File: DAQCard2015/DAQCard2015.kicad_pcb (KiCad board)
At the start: 4 copper layers, 160 x 160 mm, 191 parts, among them CON1 BARREL_JACK, K1 1462042-8, P1 QTH-090-01-F-D-A, P2 QTH-090-01-F-D-A, P3 miniDIL20, P4 LEMO_EPY.00.250.NTN, P5 LEMO_EPY.00.250.NTN, P6 FAN, P7 CONN_02X20_Double, P9 SHV, Q1 MMBT2222A-TP, Q2 SBC817-40LT1G, SW1 DPDT, U1 RJ45x8, U10 AD9219, U11 THS4524IDBTR, U12 AD9219, U13 THS4524IDBTR, U14 AD9219, U15 THS4524IDBTR, U16 AD9219, U17 THS4524IDBTR, U18 AD9219, U19 AD8534, U2 AD5628, U20 LM1086, U21 LT1913, U22 AD5628, U23 AD8534, U24 MCP65R41, U3 THS4524IDBTR, U4 AD9219, U5 THS4524IDBTR, U6 AD9219, U7 THS4524IDBTR, U8 AD9219, U9 THS4524IDBTR

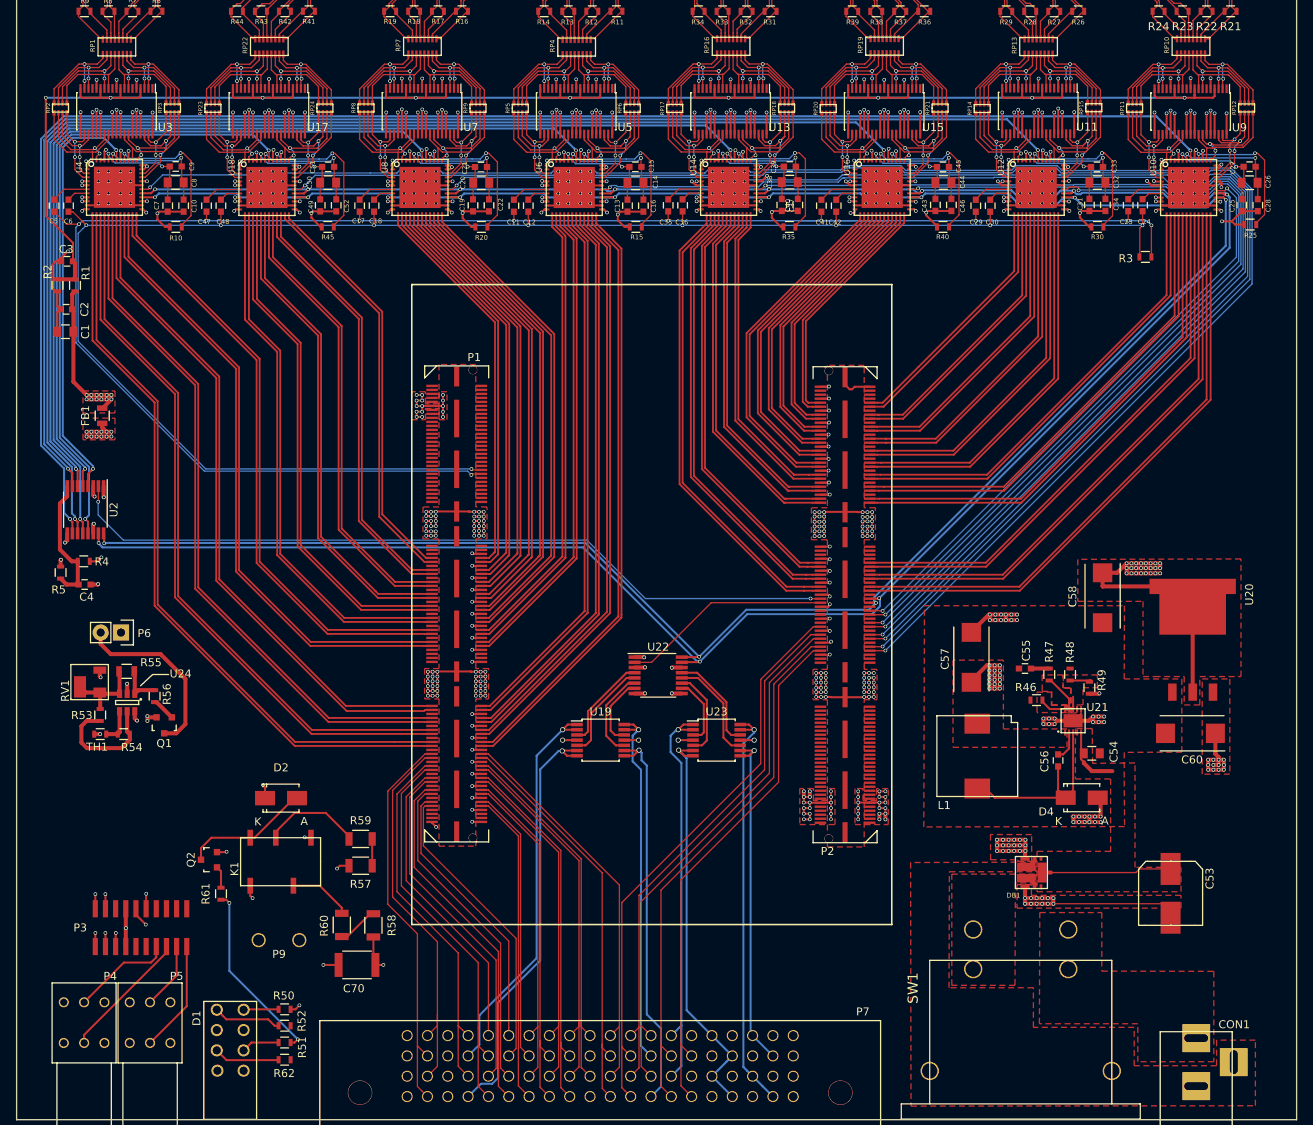
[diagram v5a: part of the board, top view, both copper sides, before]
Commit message: Update to DAQ Board including adding an JTAG header and hooking up external clock and trigger
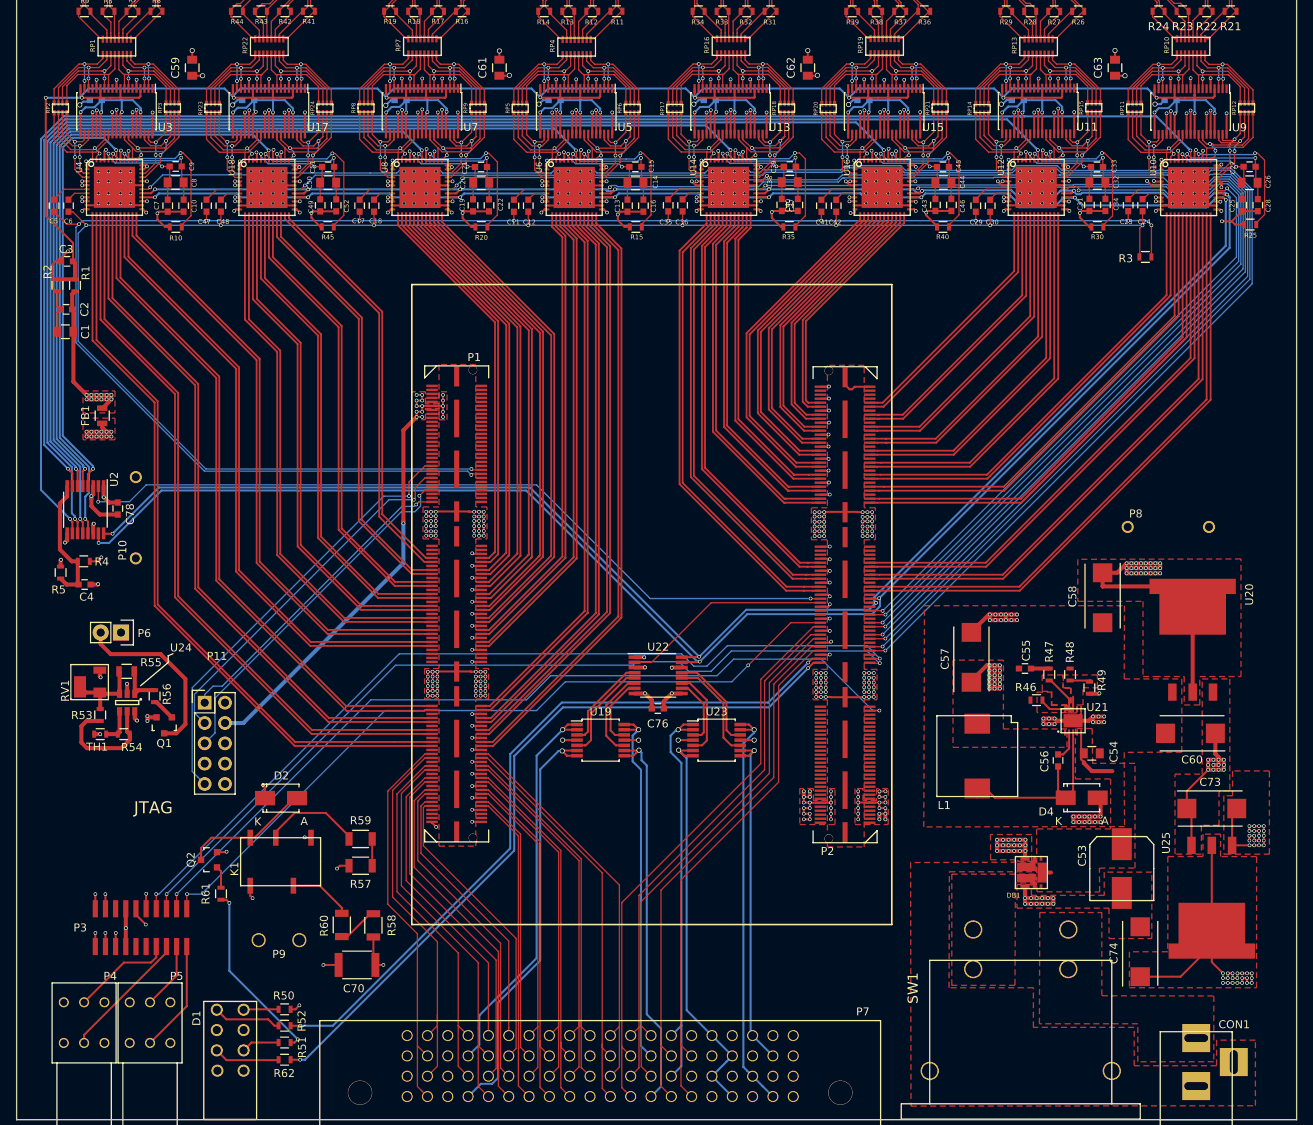
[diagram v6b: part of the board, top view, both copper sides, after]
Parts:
- added C59: 10uF, Capacitors_SMD:C_0805, F.Cu at (40.0, 52.7)
- added C61: 10uF, Capacitors_SMD:C_0805, F.Cu at (78.3, 52.7)
- added C62: 10uF, Capacitors_SMD:C_0805, F.Cu at (116.9, 52.7)
- added C63: 10uF, Capacitors_SMD:C_0805, F.Cu at (155.3, 52.7)
- added C64: .1uF, Capacitors_SMD:C_0603, B.Cu at (27.9, 56.8)
- added C65: .1uF, Capacitors_SMD:C_0603, B.Cu at (85.2, 56.8)
- added C66: .1uF, Capacitors_SMD:C_0603, B.Cu at (66.0, 56.8)
- added C67: .1uF, Capacitors_SMD:C_0603, B.Cu at (143.2, 56.8)
- added C68: .1uF, Capacitors_SMD:C_0603, B.Cu at (104.7, 56.8)
- added C69: .1uF, Capacitors_SMD:C_0603, B.Cu at (123.8, 56.8)
- added C71: .1uF, Capacitors_SMD:C_0603, B.Cu at (47.0, 56.8)
- added C72: .1uF, Capacitors_SMD:C_0603, B.Cu at (162.2, 56.8)
- added C73: 10uF, Capacitors_Tantalum_SMD:TantalC_SizeD_EIA-7343_Reflow, F.Cu at (167.4, 145.3)
- added C74: 100uF, Capacitors_Tantalum_SMD:TantalC_SizeD_EIA-7343_Reflow, F.Cu at (158.4, 163.2)
- added C76: .1uF, Capacitors_SMD:C_0603, F.Cu at (98.2, 132.8)
- added C78: .1uF, Capacitors_SMD:C_0603, F.Cu at (30.6, 107.8)
- added P10: SPYPAD, extras:Harwin_D3082-05, F.Cu at (32.9, 109.0)
- added P11: 70246-1004, Pin_Headers:Pin_Header_Straight_2x05, F.Cu at (41.5, 132.1)
- added P8: SPYPAD, extras:Harwin_D3082-05, F.Cu at (162.0, 110.1)
- added U25: LM1086_2V5, extras:TO-263-4, F.Cu at (167.4, 149.9)
- U20: value LM1086 -> LM1086_1V8
- moved C53 6.84 mm to (156.2, 152.8)
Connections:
- net Vdig renamed 2V5dig
- C3 pad 1: Vocm -> /Frontend/ADCChannel1/Vocm
- P1 pad 42: (no net) -> JTAG_TDI
- P1 pad 48: (no net) -> JTAG_TDO
- P1 pad 54: (no net) -> JTAG_TMS
- P1 pad 60: (no net) -> JTAG_TCK
- P2 pad 58: (no net) -> EXT_CLK
- P2 pad 61: (no net) -> LED1
- P2 pad 62: (no net) -> UIO_1
- P2 pad 63: (no net) -> LED0
- P2 pad 64: (no net) -> UIO_2
- P2 pad 81: (no net) -> EXT_TRG
- P3 pad 1: (no net) -> EXT_TRG
- P3 pad 3: (no net) -> EXT_CLK
- P3 pad 5: (no net) -> UIO_1
- P3 pad 7: (no net) -> UIO_2
- P7 pad 48: Vocm -> Vocm_tel
- P7 pad 49: Vocm -> Vocm_tel
- P7 pad 8: Vocm -> Vocm_tel
- P7 pad 9: Vocm -> Vocm_tel
- R1 pad 2: Vocm -> /Frontend/ADCChannel1/Vocm
- R2 pad 1: Vocm -> /Frontend/ADCChannel1/Vocm
- R52 pad 1: (no net) -> LED0
- R62 pad 1: (no net) -> LED1
- U11 pad 14: Vocm -> /Frontend/ADCChannel1/Vocm
- U11 pad 19: Vocm -> /Frontend/ADCChannel1/Vocm
- U11 pad 4: Vocm -> /Frontend/ADCChannel1/Vocm
- U11 pad 9: Vocm -> /Frontend/ADCChannel1/Vocm
- U13 pad 14: Vocm -> /Frontend/ADCChannel1/Vocm
- U13 pad 19: Vocm -> /Frontend/ADCChannel1/Vocm
- U13 pad 4: Vocm -> /Frontend/ADCChannel1/Vocm
- U13 pad 9: Vocm -> /Frontend/ADCChannel1/Vocm
- U15 pad 14: Vocm -> /Frontend/ADCChannel1/Vocm
- U15 pad 19: Vocm -> /Frontend/ADCChannel1/Vocm
- U15 pad 4: Vocm -> /Frontend/ADCChannel1/Vocm
- U15 pad 9: Vocm -> /Frontend/ADCChannel1/Vocm
- U17 pad 14: Vocm -> /Frontend/ADCChannel1/Vocm
- U17 pad 19: Vocm -> /Frontend/ADCChannel1/Vocm
- U17 pad 4: Vocm -> /Frontend/ADCChannel1/Vocm
- U17 pad 9: Vocm -> /Frontend/ADCChannel1/Vocm
- U23 pad 6: Vocm -> Vocm_tel
- U23 pad 7: Vocm -> Vocm_tel
- U3 pad 14: Vocm -> /Frontend/ADCChannel1/Vocm
- U3 pad 19: Vocm -> /Frontend/ADCChannel1/Vocm
- U3 pad 4: Vocm -> /Frontend/ADCChannel1/Vocm
- U3 pad 9: Vocm -> /Frontend/ADCChannel1/Vocm
- U5 pad 14: Vocm -> /Frontend/ADCChannel1/Vocm
- U5 pad 19: Vocm -> /Frontend/ADCChannel1/Vocm
- U5 pad 4: Vocm -> /Frontend/ADCChannel1/Vocm
- U5 pad 9: Vocm -> /Frontend/ADCChannel1/Vocm
- U7 pad 14: Vocm -> /Frontend/ADCChannel1/Vocm
- U7 pad 19: Vocm -> /Frontend/ADCChannel1/Vocm
- U7 pad 4: Vocm -> /Frontend/ADCChannel1/Vocm
- U7 pad 9: Vocm -> /Frontend/ADCChannel1/Vocm
- U9 pad 14: Vocm -> /Frontend/ADCChannel1/Vocm
- U9 pad 19: Vocm -> /Frontend/ADCChannel1/Vocm
- U9 pad 4: Vocm -> /Frontend/ADCChannel1/Vocm
- U9 pad 9: Vocm -> /Frontend/ADCChannel1/Vocm
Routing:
- net Vocm: track 316.9 -> 0.00 mm, vias 10 -> 0
- net /Frontend/ADCChannel1/Vocm: track 0.00 -> 268.6 mm, vias 0 -> 9
- net 2V5dig: track 0.00 -> 118.1 mm, vias 0 -> 21
- net UIO_2: track 0.00 -> 108.3 mm, vias 0 -> 2
- net UIO_1: track 0.00 -> 106.5 mm, vias 0 -> 2
- net EXT_CLK: track 0.00 -> 105.7 mm, vias 0 -> 2
- net 3V3ana: track 109.6 -> 212.9 mm, vias 44 -> 48
- net EXT_TRG: track 0.00 -> 95.1 mm, vias 0 -> 2
- net LED1: track 0.00 -> 93.7 mm, vias 0 -> 2
- net LED0: track 0.00 -> 92.1 mm, vias 0 -> 2
- net JTAG_TDI: track 0.00 -> 55.2 mm, vias 0 -> 1
- net Vocm_tel: track 0.00 -> 52.1 mm, vias 0 -> 1
- net 1V8dig: track 24.3 -> 73.8 mm, vias 31 -> 32
- net JTAG_TDO: track 0.00 -> 45.8 mm, vias 0 -> 1
- net JTAG_TMS: track 0.00 -> 45.1 mm, vias 0 -> 1
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- added copper zone on F.Cu, net 2V5dig
- added copper zone on POWER.Cu, net 2V5dig
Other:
- board text added: "JTAG"

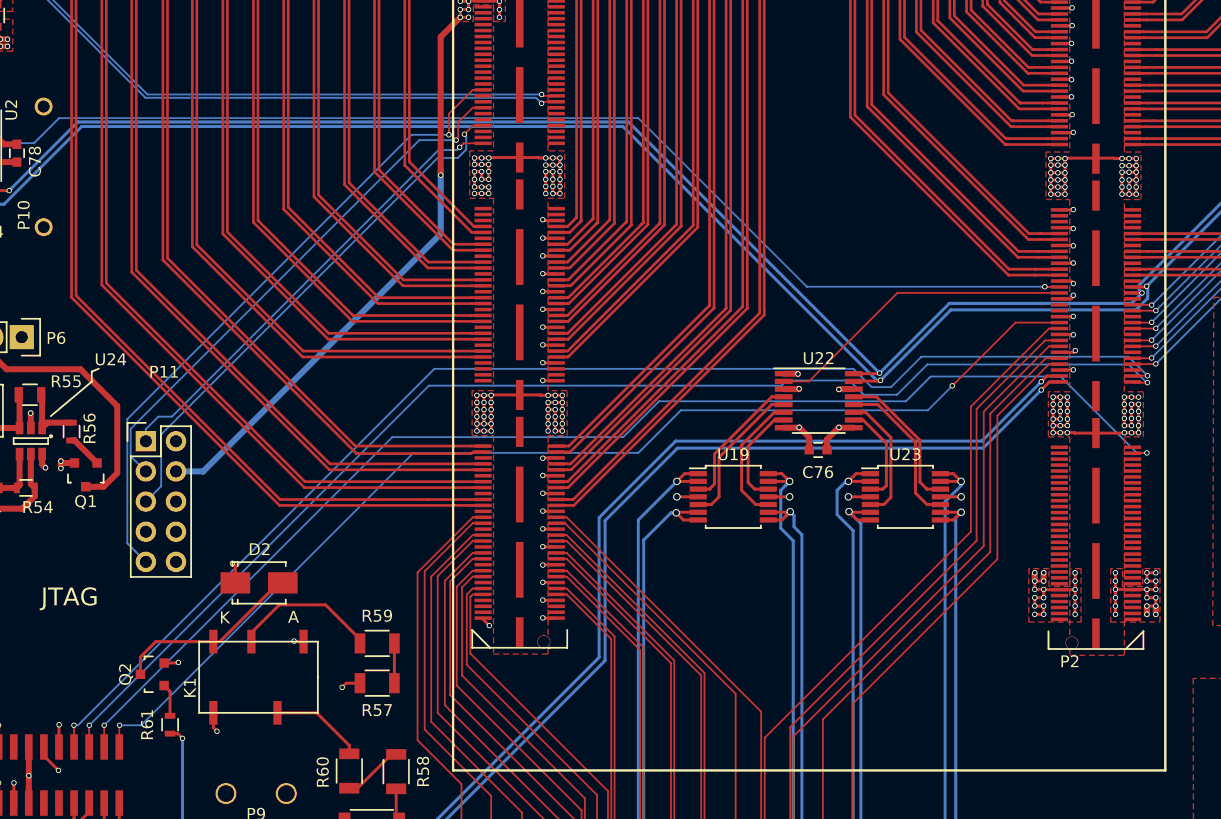
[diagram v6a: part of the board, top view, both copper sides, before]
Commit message: Moves external clock to dedicated clock input
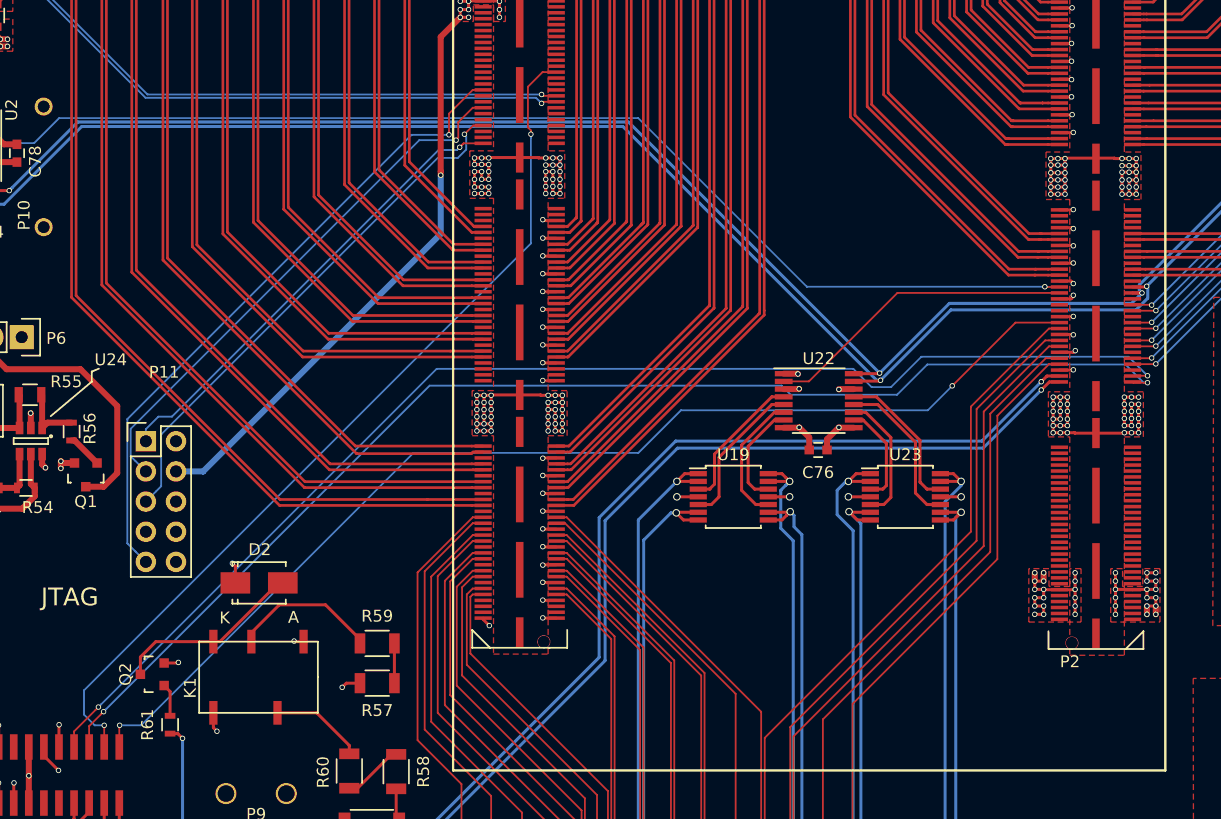
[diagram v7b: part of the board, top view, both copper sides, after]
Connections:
- P1 pad 35: (no net) -> EXT_CLK
- P2 pad 58: EXT_CLK -> (no net)
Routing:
- net EXT_CLK: track 105.7 -> 75.4 mm
